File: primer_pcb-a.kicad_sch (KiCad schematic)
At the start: 14 parts, among them J1 Pinheader - muški, J2 Pinheader - ženski, J3 Pinheader - ženski, J4 Pinheader - muški, J5 Pinheader - ženski, J6 Pinheader - muški, J7 Pinheader - ženski, J8 Pinheader - ženski, Q2 BD910, Q3 BD909

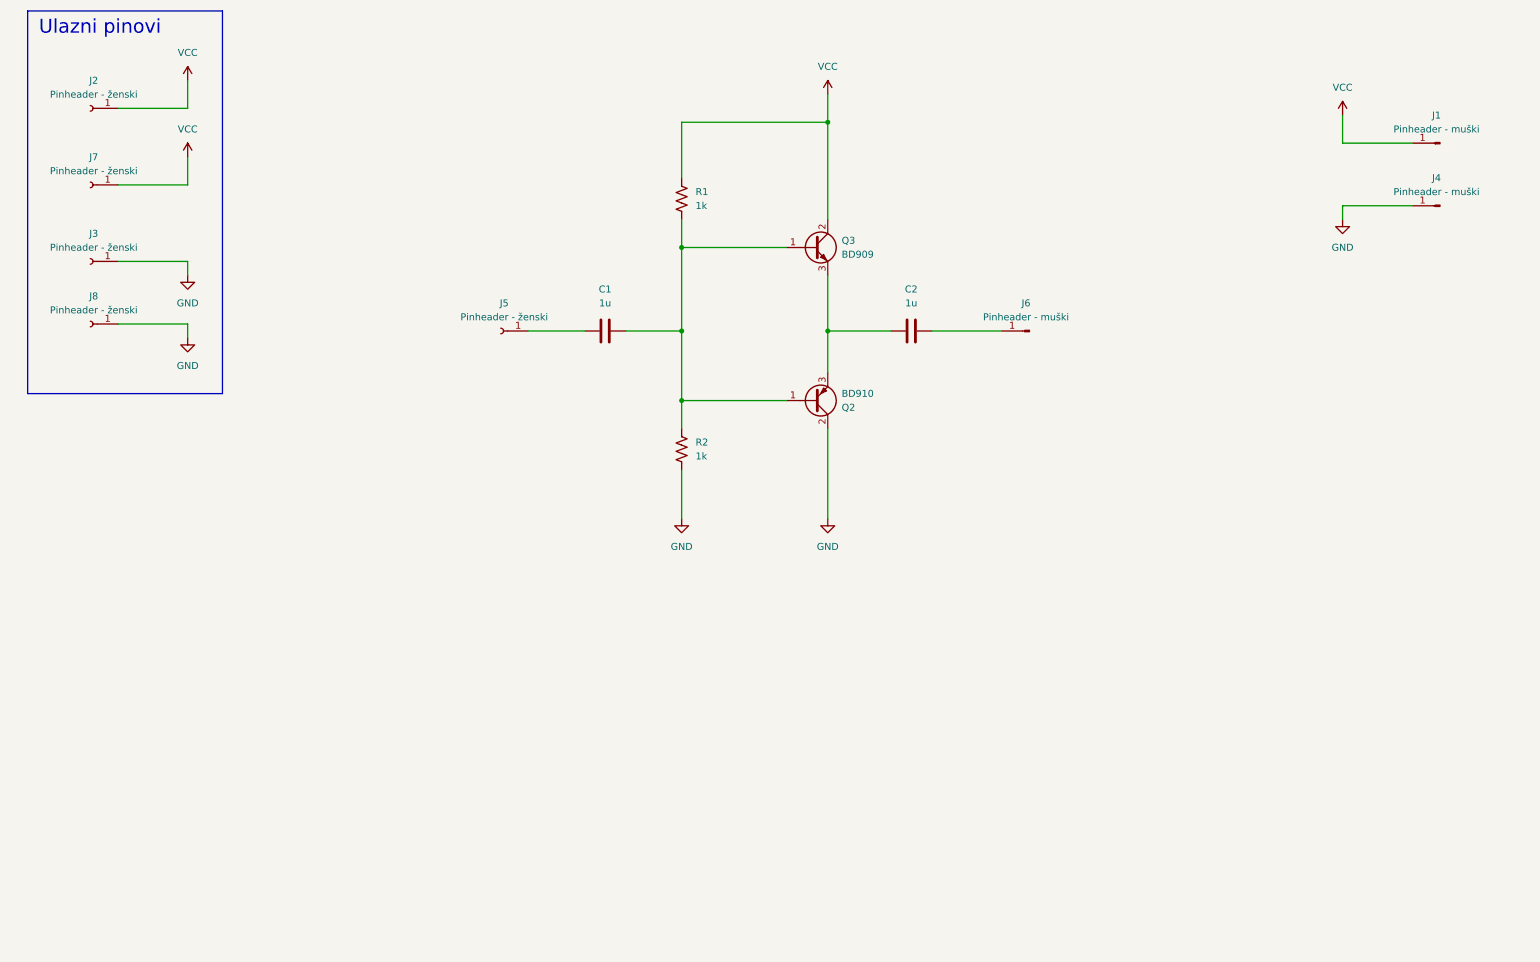
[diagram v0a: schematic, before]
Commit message: New footprints, new connectors.
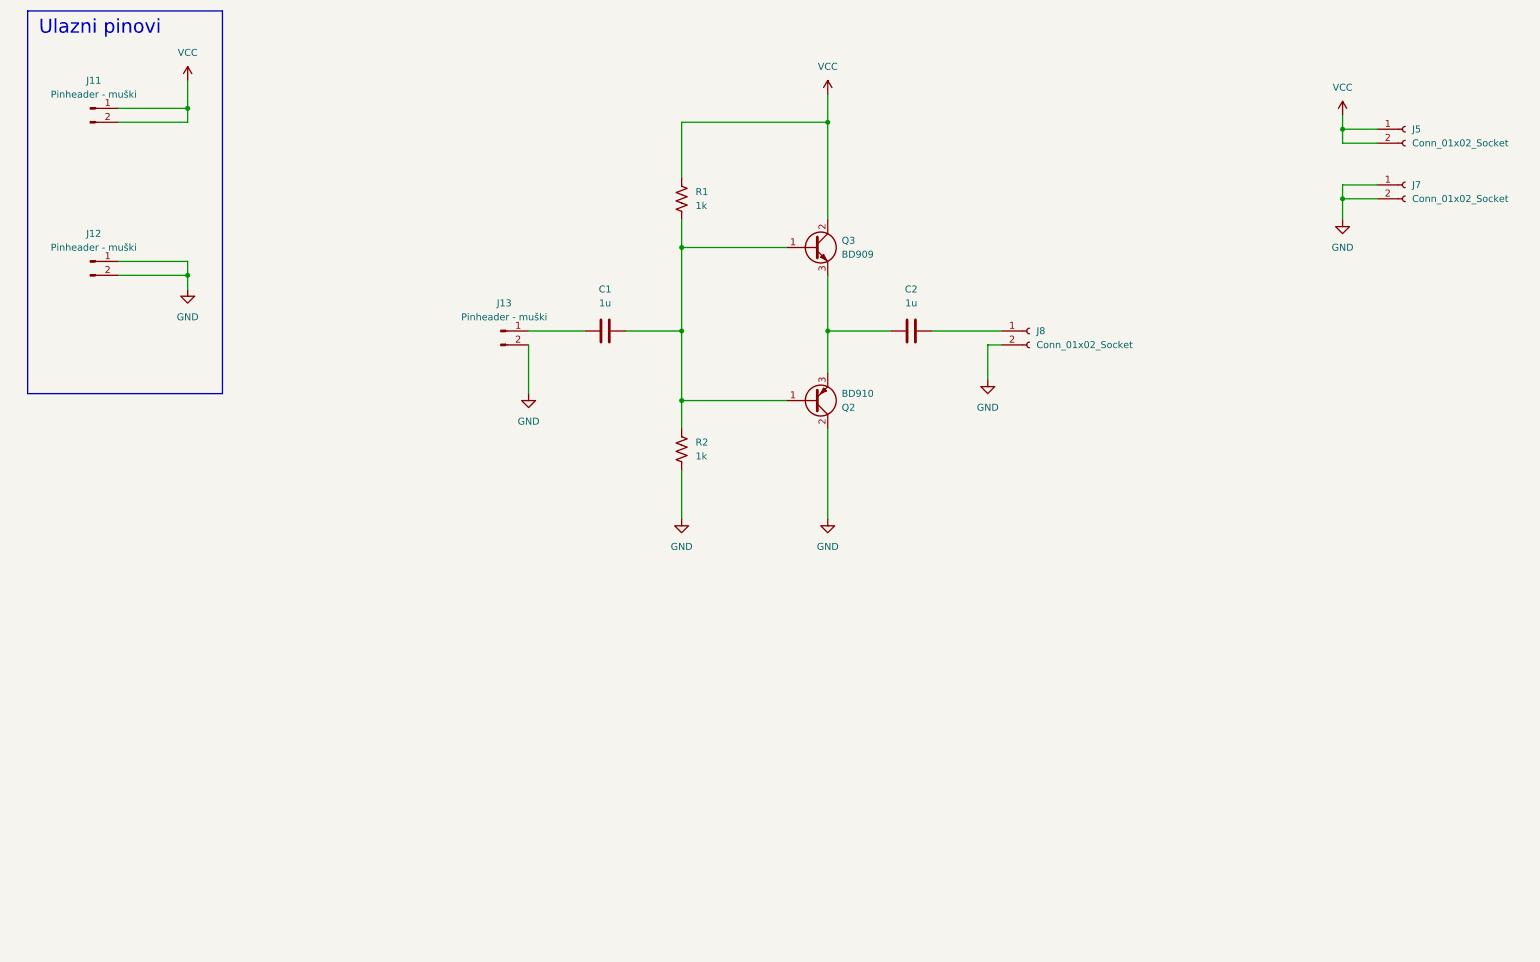
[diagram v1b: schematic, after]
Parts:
- removed J1, J4, J6: Pinheader - muški, Connector_PinHeader_2.54mm:PinHeader_1x01_P2.54mm_Horizontal, symbol Connector:Conn_01x01_Pin
- removed J2, J3, J5, J7, J8: Pinheader - ženski, Connector_PinSocket_2.54mm:PinSocket_1x01_P2.54mm_Horizontal, symbol Connector:Conn_01x01_Socket
- added J11, J12, J13: Pinheader - muški, primer_lib:PinHeader_1x02_P2.54mm_Polegnut, symbol Connector:Conn_01x02_Pin
- added J5, J7, J8: Conn_01x02_Socket, primer_lib:PinSocket_1x02_P2.54mm_Polegnut, symbol Connector:Conn_01x02_Socket
- C1, C2: footprint (none) -> Capacitor_SMD:C_1206_3216Metric_Pad1.33x1.80mm_HandSolder
- R1, R2: footprint (none) -> Resistor_SMD:R_1206_3216Metric_Pad1.30x1.75mm_HandSolder
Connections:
- net GND: now also J12.1 (Pin_1), J12.2 (Pin_2), J13.2 (Pin_2), J7.1 (Pin_1), J7.2 (Pin_2), J8.2 (Pin_2)
- net VCC: now also J11.1 (Pin_1), J11.2 (Pin_2), J5.1 (Pin_1), J5.2 (Pin_2)
- net at C1.1: now also J13.1 (Pin_1)
- net at C2.2: now also J8.1 (Pin_1)

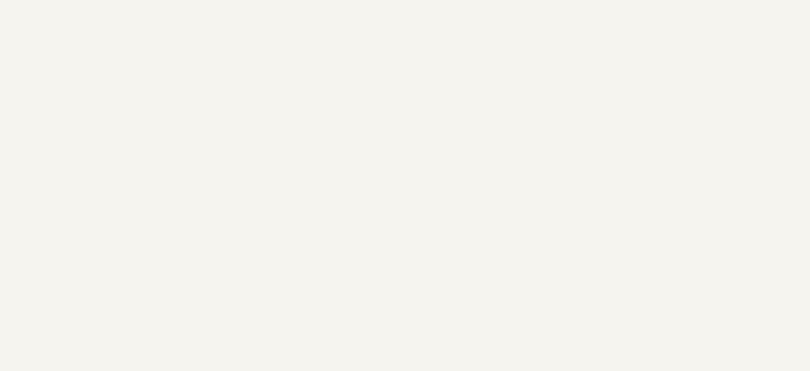
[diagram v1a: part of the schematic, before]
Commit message: Added mounting holes.
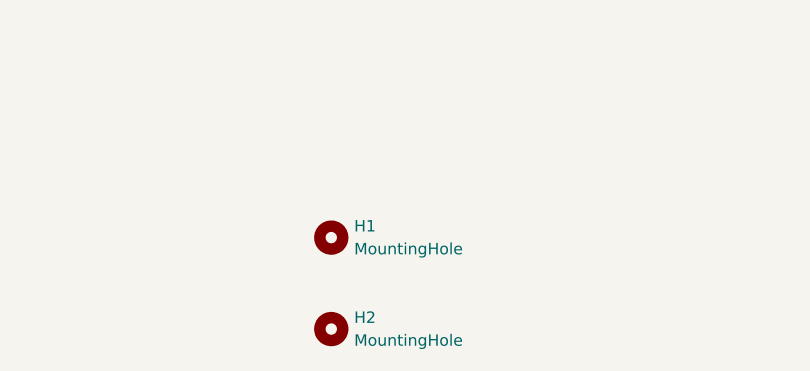
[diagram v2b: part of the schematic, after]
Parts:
- added H1, H2: MountingHole, MountingHole:MountingHole_3.2mm_M3, symbol Mechanical:MountingHole
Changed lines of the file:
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@@
+	)
+	(symbol
+		(lib_id "Mechanical:MountingHole")
+		(at 123.19 181.61 0)
+		(unit 1)
+		(exclude_from_sim no)
+		(in_bom no)
+		(on_board yes)
+		(dnp no)
+		(fields_autoplaced yes)
+		(property "Reference" "H2"
+			(at 125.73 180.3399 0)
+			(effects
+				(font
+					(size 1.27 1.27)
+				)
+				(justify left)
+			)
+		)
+		(property "Value" "MountingHole"
+			(at 125.73 182.8799 0)
+			(effects
+				(font
+					(size 1.27 1.27)
+				)
+				(justify left)
+			)
+		)
+		(property "Footprint" "MountingHole:MountingHole_3.2mm_M3"
+			(at 123.19 181.61 0)
+			(effects
+				(font
+					(size 1.27 1.27)
+				)
+				(hide yes)
+			)
+		)
+		(property "Datasheet" "~"
+			(at 123.19 181.61 0)
+			(effects
+				(font
+					(size 1.27 1.27)
+				)
+				(hide yes)
+			)
+		)
+		(property "Description" "Mounting Hole without connection"
+			(at 123.19 181.61 0)
+			(effects
+				(font
+					(size 1.27 1.27)
+				)
+				(hide yes)
+			)
+		)
+		(instances
+			(project "primer_pcb-a"
+				(path "/f61be368-fbc8-4eda-847b-8d403dc60053"
+					(reference "H2")
+					(unit 1)
+				)
+			)
+		)
 	)
 	(symbol
@@
 					(unit 1)
 				)
+			)
+		)
+	)
+	(symbol
+		(lib_id "Mechanical:MountingHole")
+		(at 123.19 171.45 0)
+		(unit 1)
+		(exclude_from_sim no)
+		(in_bom no)
+		(on_board yes)
+		(dnp no)
+		(fields_autoplaced yes)
+		(property "Reference" "H1"
+			(at 125.73 170.1799 0)
+			(effects
+				(font
+					(size 1.27 1.27)
+				)
+				(justify left)
+			)
+		)
+		(property "Value" "MountingHole"
+			(at 125.73 172.7199 0)
+			(effects
+				(font
+					(size 1.27 1.27)
+				)
+				(justify left)
+			)
+		)
+		(property "Footprint" "MountingHole:MountingHole_3.2mm_M3"
+			(at 123.19 171.45 0)
+			(effects
+				(font
+					(size 1.27 1.27)
+				)
+				(hide yes)
+			)
+		)
+		(property "Datasheet" "~"
+			(at 123.19 171.45 0)
+			(effects
+				(font
+					(size 1.27 1.27)
+				)
+				(hide yes)
+			)
+		)
+		(property "Description" "Mounting Hole without connection"
+			(at 123.19 171.45 0)
+			(effects
+				(font
+					(size 1.27 1.27)
+				)
+				(hide yes)
+			)
+		)
+		(instances
+			(project ""
+				(path "/f61be368-fbc8-4eda-847b-8d403dc60053"
+					(reference "H1")
+					(unit 1)
+				)

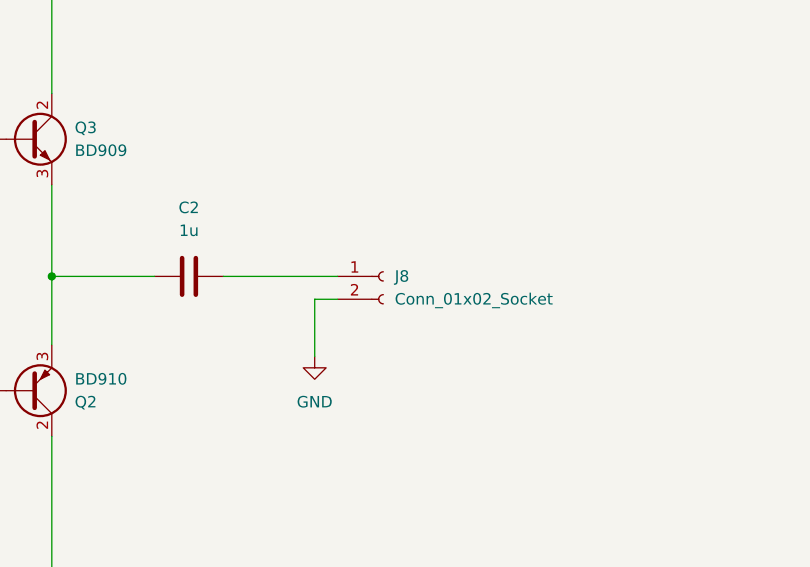
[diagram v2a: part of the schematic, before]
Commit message: Updated pins
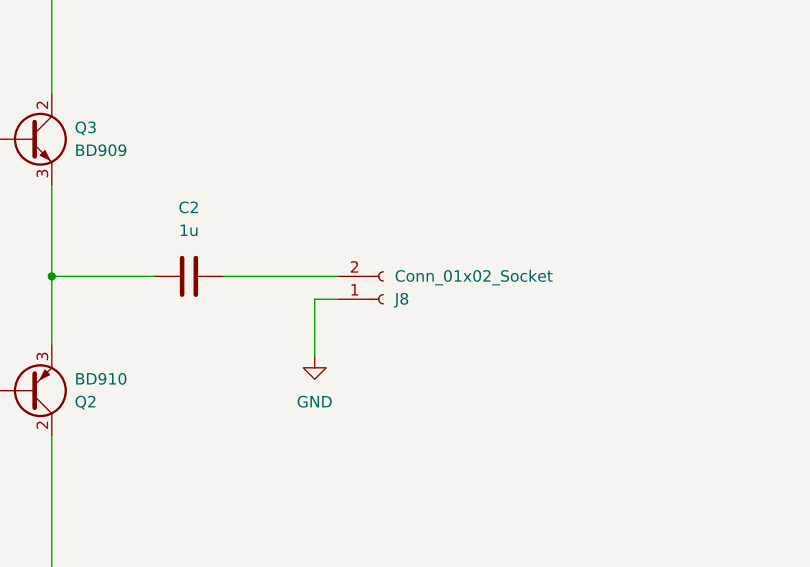
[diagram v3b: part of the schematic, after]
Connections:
- net GND: now also J8.1 (Pin_1); no longer J8.2 (Pin_2)
- net at C2.2: now also J8.2 (Pin_2); no longer J8.1 (Pin_1)
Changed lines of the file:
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@@
 	(wire
 		(pts
-			(xy 177.8 71.12) (xy 190.5 71.12)
+			(xy 190.5 71.12) (xy 177.8 71.12)
 		)
 		(stroke
@@
 	(symbol
 		(lib_id "Connector:Conn_01x02_Socket")
-		(at 195.58 71.12 0)
+		(at 195.58 73.66 0)
+		(mirror x)
 		(unit 1)
 		(exclude_from_sim no)
@@
 		(on_board yes)
 		(dnp no)
-		(fields_autoplaced yes)
 		(property "Reference" "J8"
-			(at 196.85 71.1199 0)
+			(at 196.85 73.6601 0)
 			(effects
 				(font
@@
 		)
 		(property "Value" "Conn_01x02_Socket"
-			(at 196.85 73.6599 0)
+			(at 196.85 71.1201 0)
 			(effects
 				(font
@@
 		)
 		(property "Footprint" "primer_lib:PinSocket_1x02_P2.54mm_Polegnut"
-			(at 195.58 71.12 0)
+			(at 195.58 73.66 0)
 			(effects
 				(font
@@
 		)
 		(property "Datasheet" "~"
-			(at 195.58 71.12 0)
+			(at 195.58 73.66 0)
 			(effects
 				(font
@@
 		)
 		(property "Description" "Generic connector, single row, 01x02, script generated"
-			(at 195.58 71.12 0)
-			(effects
-				(font
+			(at 195.58 73.66 0)
+			(effects
+				(font
